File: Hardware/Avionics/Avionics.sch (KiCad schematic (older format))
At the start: 31 parts

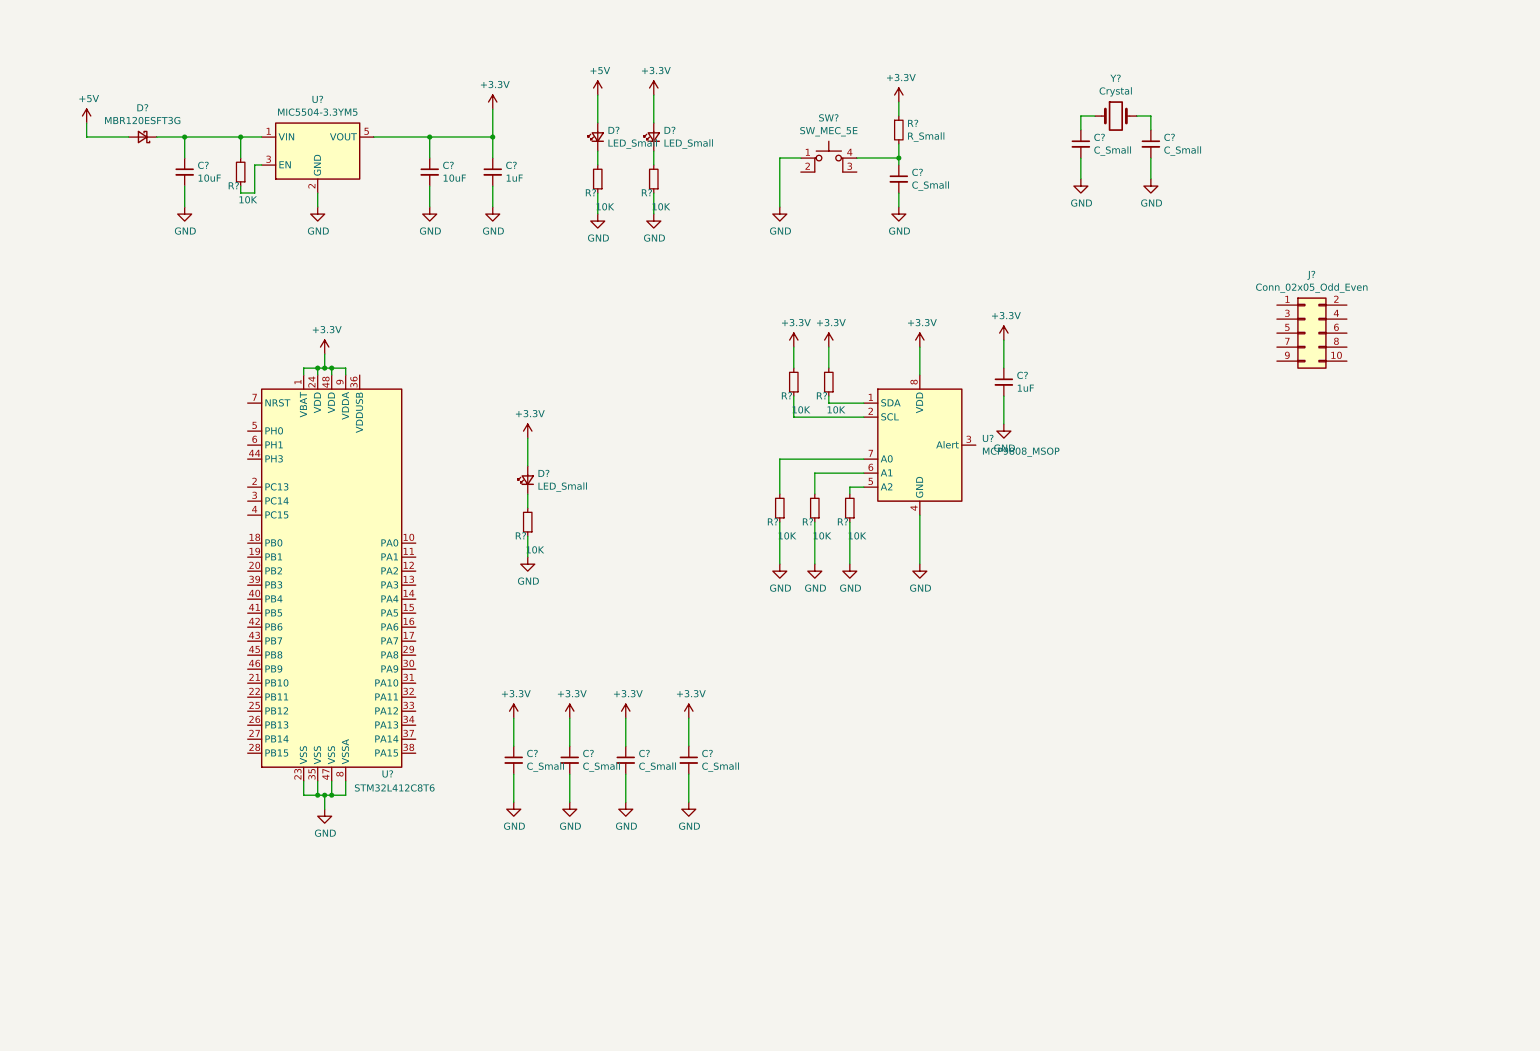
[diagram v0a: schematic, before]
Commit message: Added SPI Flash, Voltage LEDs, User LED, Reset Button, BOOT 0 Button, USB Mini Connector, Pin Headers
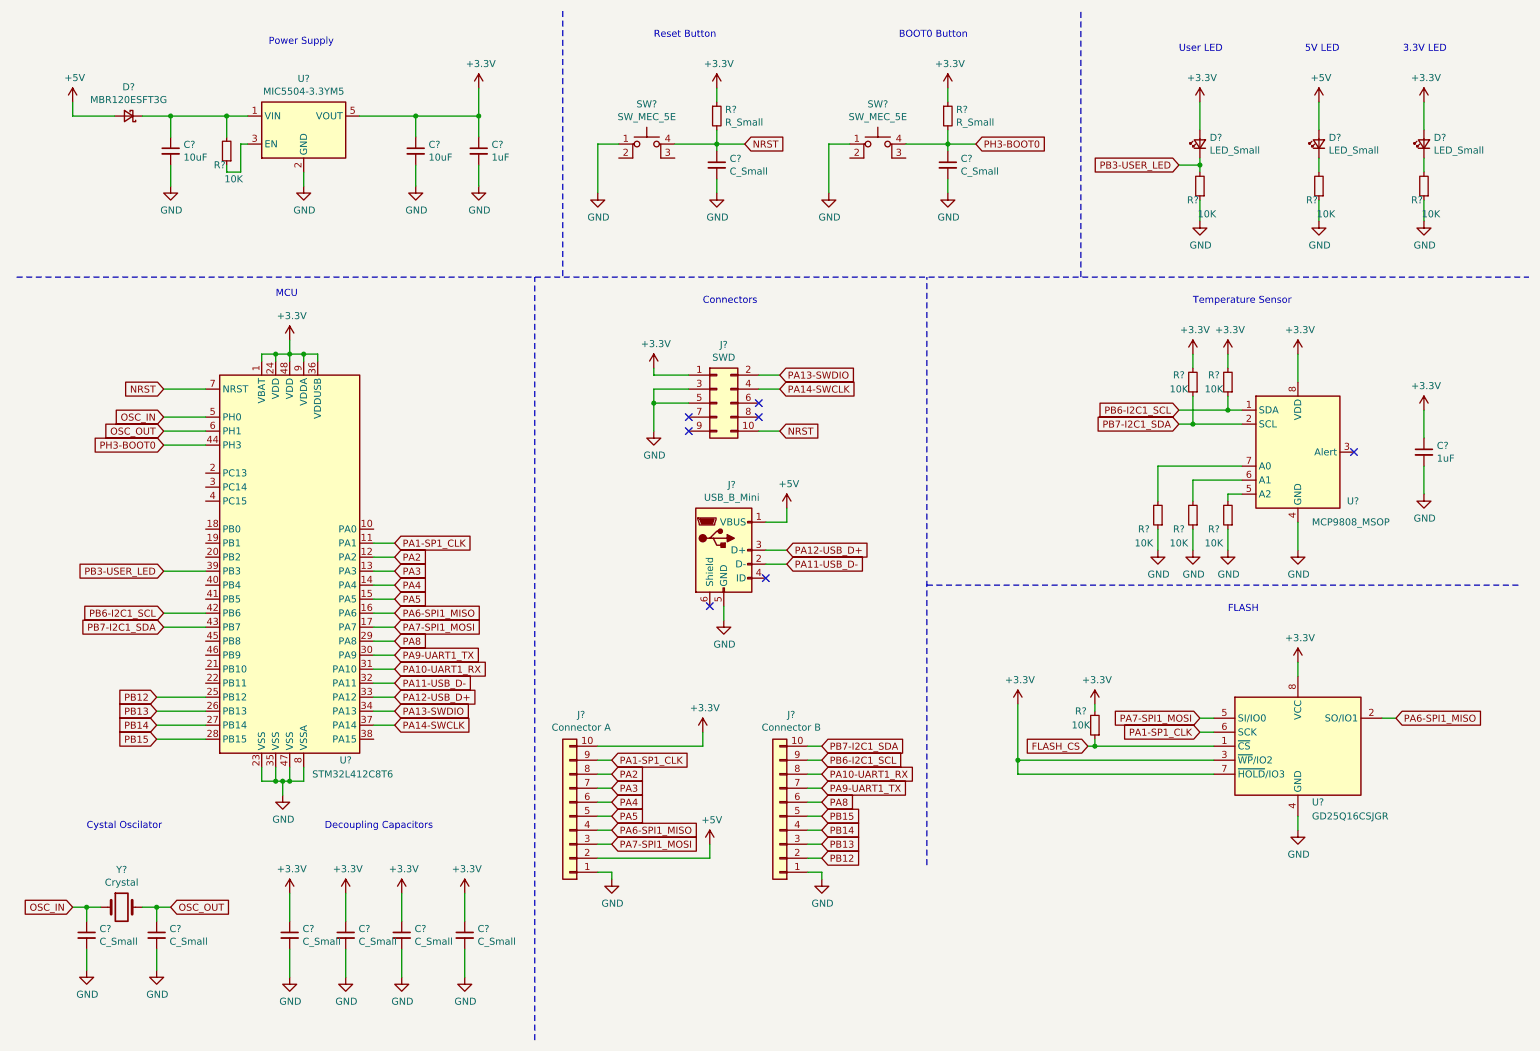
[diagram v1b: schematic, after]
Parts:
- added C?: C_Small, symbol Device:C_Small
- added J?: USB_B_Mini, symbol Connector:USB_B_Mini
- added J?: Connector A, symbol Connector_Generic:Conn_01x10
- added J?: Connector B, symbol Connector_Generic:Conn_01x10
- added R?: 10K, symbol Device:R_Small
- added R?: R_Small, symbol Device:R_Small
- added SW?: SW_MEC_5E, symbol Switch:SW_MEC_5E
- added U?: GD25Q16CSJGR, Package_SO:SOIC-8_3.9x4.9mm_P1.27mm, symbol Memory_Flash:AT25SF081-SSHD-X
- J?: value Conn_02x05_Odd_Even -> SWD
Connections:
- net +3V3: now also J?.1 (Pin_1), U?.36 (VDDUSB), J?.10 (Pin_10), R?.1, R?.2, U?.3 (~WP~/IO2), U?.7 (~HOLD~/IO3), U?.8 (VCC)
- net +5V: now also J?.1 (VBUS), J?.2 (Pin_2)
- net GND: now also J?.3 (Pin_3), J?.5 (Pin_5), C?.2, J?.1 (Pin_1), J?.1 (Pin_1), J?.5 (GND), SW?.1, U?.4 (GND)
- net PA1-SP1_CLK: now reaches U?.11 (PA1)
- net PA1-SP1_CLK: now also J?.9 (Pin_9), U?.6 (SCK)
- net PA2: now reaches U?.12 (PA2)
- net PA2: now also J?.8 (Pin_8)
- net PA3: now reaches U?.13 (PA3)
- net PA3: now also J?.7 (Pin_7)
- net PA4: now reaches U?.14 (PA4)
- net PA4: now also J?.6 (Pin_6)
- net PA5: now reaches U?.15 (PA5)
- net PA5: now also J?.5 (Pin_5)
- net PA6-SPI1_MISO: now reaches U?.16 (PA6)
- net PA6-SPI1_MISO: now also J?.4 (Pin_4), U?.2 (SO/IO1)
- net PA7-SPI1_MOSI: now reaches U?.17 (PA7)
- net PA7-SPI1_MOSI: now also J?.3 (Pin_3), U?.5 (SI/IO0)
- net PB12: now reaches U?.25 (PB12)
- net PB12: now also J?.2 (Pin_2)
- net PB13: now reaches U?.26 (PB13)
- net PB13: now also J?.3 (Pin_3)
- net PB14: now reaches U?.27 (PB14)
- net PB14: now also J?.4 (Pin_4)
- net PB15: now reaches U?.28 (PB15)
- net PB15: now also J?.5 (Pin_5)
- net PA8: now reaches U?.29 (PA8)
- net PA8: now also J?.6 (Pin_6)
- net PA9-UART1_TX: now reaches U?.30 (PA9)
- net PA9-UART1_TX: now also J?.7 (Pin_7)
- net PA10-UART1_RX: now reaches U?.31 (PA10)
- net PA10-UART1_RX: now also J?.8 (Pin_8)
- net PA11-USB_D-: now reaches U?.32 (PA11)
- net PA11-USB_D-: now also J?.2 (D-)
- net PA12-USB_D+: now reaches U?.33 (PA12)
- net PA12-USB_D+: now also J?.3 (D+)
- net PA13-SWDIO: now reaches U?.34 (PA13)
- net PA13-SWDIO: now also J?.2 (Pin_2)
- net PA14-SWCLK: now reaches U?.37 (PA14)
- net PA14-SWCLK: now also J?.4 (Pin_4)
- net PB3-USER_LED: now reaches U?.39 (PB3)
- net PB3-USER_LED: now also D?.1 (K), R?.2
- net PB6-I2C1_SCL: now reaches U?.42 (PB6)
- net PB6-I2C1_SCL: now also R?.1, U?.1 (SDA), J?.9 (Pin_9)
- net PB7-I2C1_SDA: now reaches U?.43 (PB7)
- net PB7-I2C1_SDA: now also R?.1, U?.2 (SCL), J?.10 (Pin_10)
- net PH3-BOOT0: now reaches U?.44 (PH3)
- net PH3-BOOT0: now also C?.1, R?.2, SW?.4 (A)
- net OSC_IN: now reaches U?.5 (PH0)
- net OSC_IN: now also C?.1, Y?.1
- net OSC_OUT: now reaches U?.6 (PH1)
- net OSC_OUT: now also C?.1, Y?.2
- net NRST: now reaches U?.7 (NRST)
- net NRST: now also C?.1, J?.10 (Pin_10), R?.2, SW?.4 (A)
- new net FLASH_CS: R?.1, U?.1 (~CS)
- no-connect marks 0 -> 7
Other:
- note added: "3.3V LED"
- note added: "5V LED"
- note added: "BOOT0 Button"
- note added: "Connectors"
- note added: "Cystal Oscilator"
- note added: "Decoupling Capacitors"
- note added: "FLASH"
- note added: "MCU"
- note added: "Power Supply"
- note added: "Reset Button"
- note added: "Temperature Sensor"
- note added: "User LED"
- moved on the sheet: C?, D?, J?, R?, SW?, U?, Y?

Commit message: Finished schematic connections, assigning of component name and value, selection of footprints, sheet specification
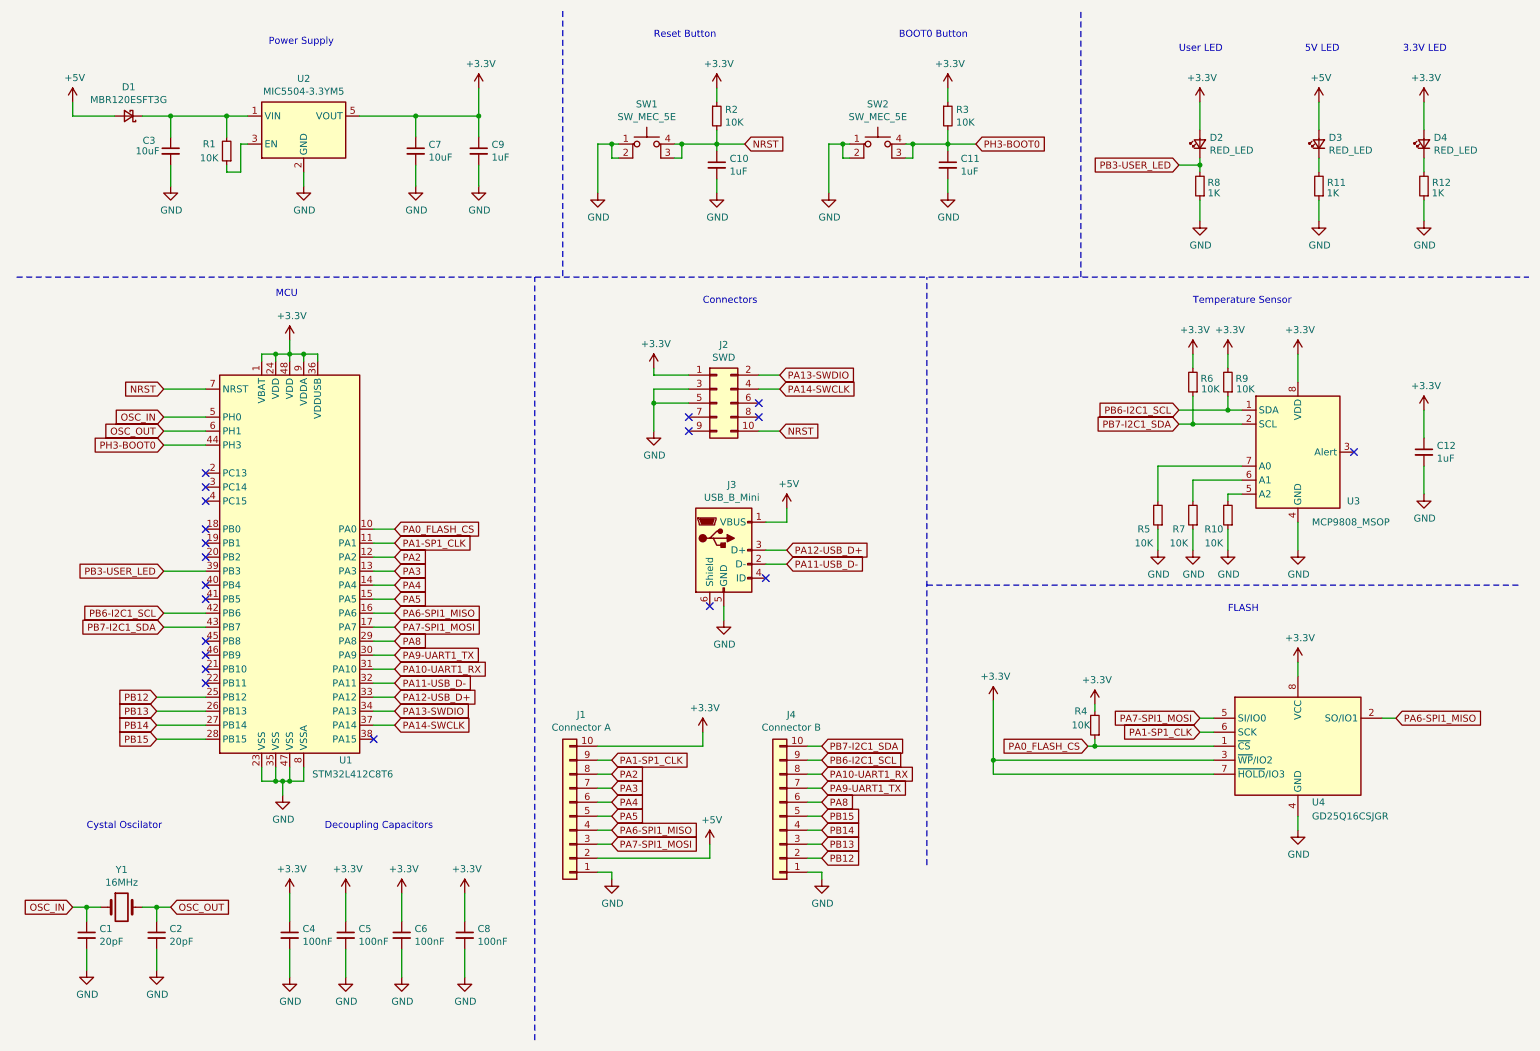
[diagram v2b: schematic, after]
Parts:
- C1: renamed from C?; value C_Small -> 20pF; footprint (none) -> Capacitor_SMD:C_0805_2012Metric_Pad1.18x1.45mm_HandSolder
- C10, C11: renamed from C?; value C_Small -> 1uF; footprint (none) -> Capacitor_SMD:C_01005_0402Metric_Pad0.57x0.30mm_HandSolder
- C12, C3, C7, C9: renamed from C?; footprint (none) -> Capacitor_SMD:C_01005_0402Metric_Pad0.57x0.30mm_HandSolder
- C2: renamed from C?; value C_Small -> 20pF; footprint (none) -> Capacitor_SMD:C_01005_0402Metric_Pad0.57x0.30mm_HandSolder
- C4, C5, C6, C8: renamed from C?; value C_Small -> 100nF; footprint (none) -> Capacitor_SMD:C_01005_0402Metric_Pad0.57x0.30mm_HandSolder
- D1: renamed from D?; footprint (none) -> Diode_SMD:D_SOD-123F
- D2, D3, D4: renamed from D?; value LED_Small -> RED_LED; footprint (none) -> LED_SMD:LED_0805_2012Metric_Pad1.15x1.40mm_HandSolder
- J1: renamed from J?; footprint (none) -> Connector_PinHeader_2.54mm:PinHeader_1x10_P2.54mm_Horizontal
- J2: renamed from J?; footprint (none) -> Connector_PinHeader_1.27mm:PinHeader_2x05_P1.27mm_Vertical
- J3: renamed from J?; footprint (none) -> Connector_USB:USB_Micro-B_Amphenol_10103594-0001LF_Horizontal
- J4: renamed from J?; footprint (none) -> Connector_PinHeader_2.54mm:PinHeader_1x10_P2.54mm_Vertical
- R1, R10, R4, R5, R6, R7, R9: renamed from R?; footprint (none) -> Resistor_SMD:R_0805_2012Metric_Pad1.20x1.40mm_HandSolder
- R11, R12, R8: renamed from R?; value 10K -> 1K; footprint (none) -> Resistor_SMD:R_0805_2012Metric_Pad1.20x1.40mm_HandSolder
- R2, R3: renamed from R?; value R_Small -> 10K; footprint (none) -> Resistor_SMD:R_0805_2012Metric_Pad1.20x1.40mm_HandSolder
- SW1, SW2: renamed from SW?; footprint (none) -> Button_Switch_SMD:SW_SPST_Omron_B3FS-100xP
- U4: renamed from U?; footprint Package_SO:SOIC-8_3.9x4.9mm_P1.27mm -> Package_SO:SOP-8_5.28x5.23mm_P1.27mm
- Y1: renamed from Y?; value Crystal -> 16MHz; footprint (none) -> Crystal:Crystal_HC49-U_Vertical
- gave numbers to parts that had none: 3
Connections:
- net FLASH_CS is gone; now on net PA0_FLASH_CS: R4.1, U4.1 (~CS)
- net GND: now also SW1.2, SW2.2
- net NRST: now also SW1.3 (K)
- net PH3-BOOT0: now also SW2.3 (K)
- net PA0_FLASH_CS: now reaches U1.10 (PA0)
- no-connect marks 7 -> 20

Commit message: Added PCB desgin, modification on the schematic for a better pcb layout, generation of Gerber files and BOM. In this commit the PCB design files where sent to manufacture and the components where ordered from mouser.
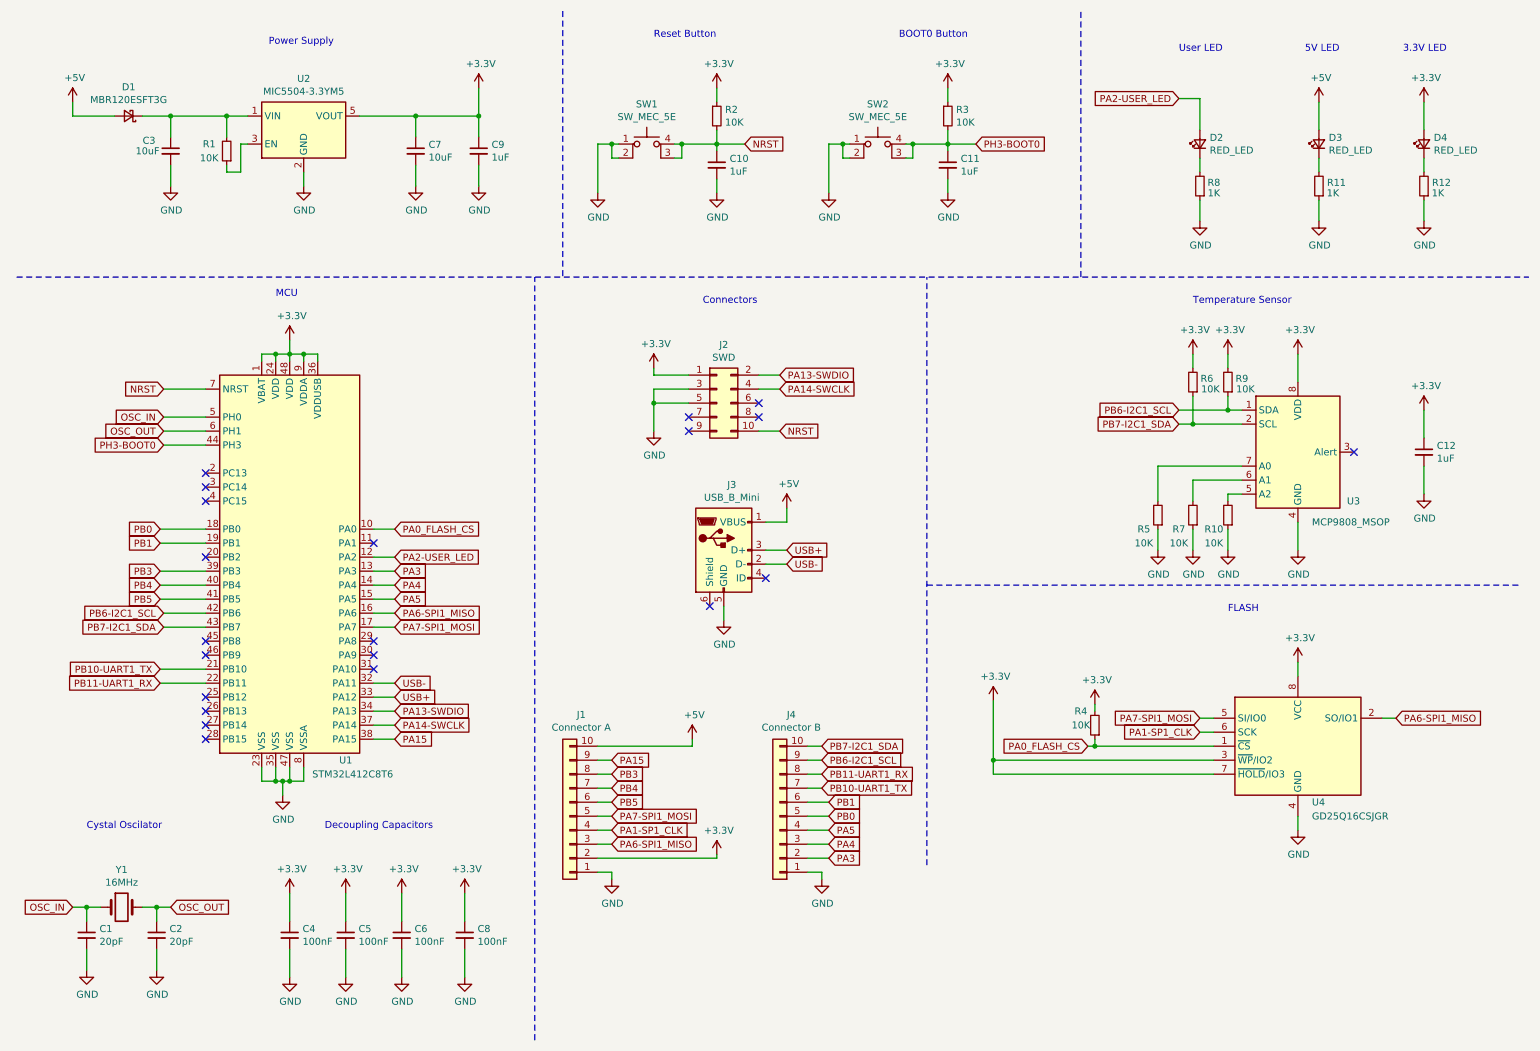
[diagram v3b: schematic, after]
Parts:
- C10, C11, C12, C2, C3, C4, C5, C6, C7, C8, C9: footprint Capacitor_SMD:C_01005_0402Metric_Pad0.57x0.30mm_HandSolder -> Capacitor_SMD:C_0805_2012Metric_Pad1.18x1.45mm_HandSolder
- J1: footprint Connector_PinHeader_2.54mm:PinHeader_1x10_P2.54mm_Horizontal -> Connector_PinHeader_2.54mm:PinHeader_1x10_P2.54mm_Vertical
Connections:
- net +3V3: now also J1.2 (Pin_2); no longer D2.2 (A), J1.10 (Pin_10)
- net +5V: now also J1.10 (Pin_10); no longer J1.2 (Pin_2)
- net PA1-SP1_CLK: now also J1.4 (Pin_4); no longer J1.9 (Pin_9), U1.11 (PA1)
- net PA3: now also J4.2 (Pin_2); no longer J1.7 (Pin_7)
- net PA4: now also J4.3 (Pin_3); no longer J1.6 (Pin_6)
- net PA5: now also J4.4 (Pin_4); no longer J1.5 (Pin_5)
- net PA6-SPI1_MISO: now also J1.3 (Pin_3); no longer J1.4 (Pin_4)
- net PA7-SPI1_MOSI: now also J1.5 (Pin_5); no longer J1.3 (Pin_3)
- net PB0: now reaches U1.18 (PB0)
- net PB0: now also J4.5 (Pin_5)
- net PB1: now reaches U1.19 (PB1)
- net PB1: now also J4.6 (Pin_6)
- net PB10-UART1_TX: now reaches U1.21 (PB10)
- net PB10-UART1_TX: now also J4.7 (Pin_7)
- net PB11-UART1_RX: now reaches U1.22 (PB11)
- net PB11-UART1_RX: now also J4.8 (Pin_8)
- net PA15: now reaches U1.38 (PA15)
- net PA15: now also J1.9 (Pin_9)
- net PB4: now reaches U1.40 (PB4)
- net PB4: now also J1.7 (Pin_7)
- net PB5: now reaches U1.41 (PB5)
- net PB5: now also J1.6 (Pin_6)
- net PA10-UART1_RX: no longer names the net of U1.31 (PA10)
- net PA10-UART1_RX: no longer J4.8 (Pin_8)
- net PA11-USB_D- renamed USB-
- net PA12-USB_D+ renamed USB+
- net PA2 renamed PA2-USER_LED
- net PA2-USER_LED: now also D2.2 (A); no longer J1.8 (Pin_8)
- net PA8: no longer names the net of U1.29 (PA8)
- net PA8: no longer J4.6 (Pin_6)
- net PA9-UART1_TX: no longer names the net of U1.30 (PA9)
- net PA9-UART1_TX: no longer J4.7 (Pin_7)
- net PB12: no longer names the net of U1.25 (PB12)
- net PB12: no longer J4.2 (Pin_2)
- net PB13: no longer names the net of U1.26 (PB13)
- net PB13: no longer J4.3 (Pin_3)
- net PB14: no longer names the net of U1.27 (PB14)
- net PB14: no longer J4.4 (Pin_4)
- net PB15: no longer names the net of U1.28 (PB15)
- net PB15: no longer J4.5 (Pin_5)
- net PB3-USER_LED: no longer names the net of D2.1 (K), R8.2
- net PB3-USER_LED: no longer U1.39 (PB3)
- new net PB3: J1.8 (Pin_8), U1.39 (PB3)
- no-connect marks 20 -> 21
